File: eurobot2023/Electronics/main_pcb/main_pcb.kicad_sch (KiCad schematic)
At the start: 34 parts, among them IC1 CD74HCT125M96, IC2 SN74LVC126ADR, J1 PI40HAT, J10 Conn_01x02_Male, J11 MagneticEncoder, J12 Conn_01x07_Male, J13 MagneticEncoder, J14 Conn_01x03_Male, J15 Conn_01x02_Male, J2 Conn_01x02_Male, J3 Conn_01x02_Male, J4 Conn_01x02_Male, J5 Conn_01x02_Male, J6 Conn_01x02_Male, J7 Conn_01x02_Male, J9 22-03-5035, P1 R-78Bxx-2.0, P2 Amazon 5A stepdown, U1 MCP2515-xSO, U2 TJA1049T, U3 PCA9306D, U4 Pololu_MAX14870, U5 PCA9685PW

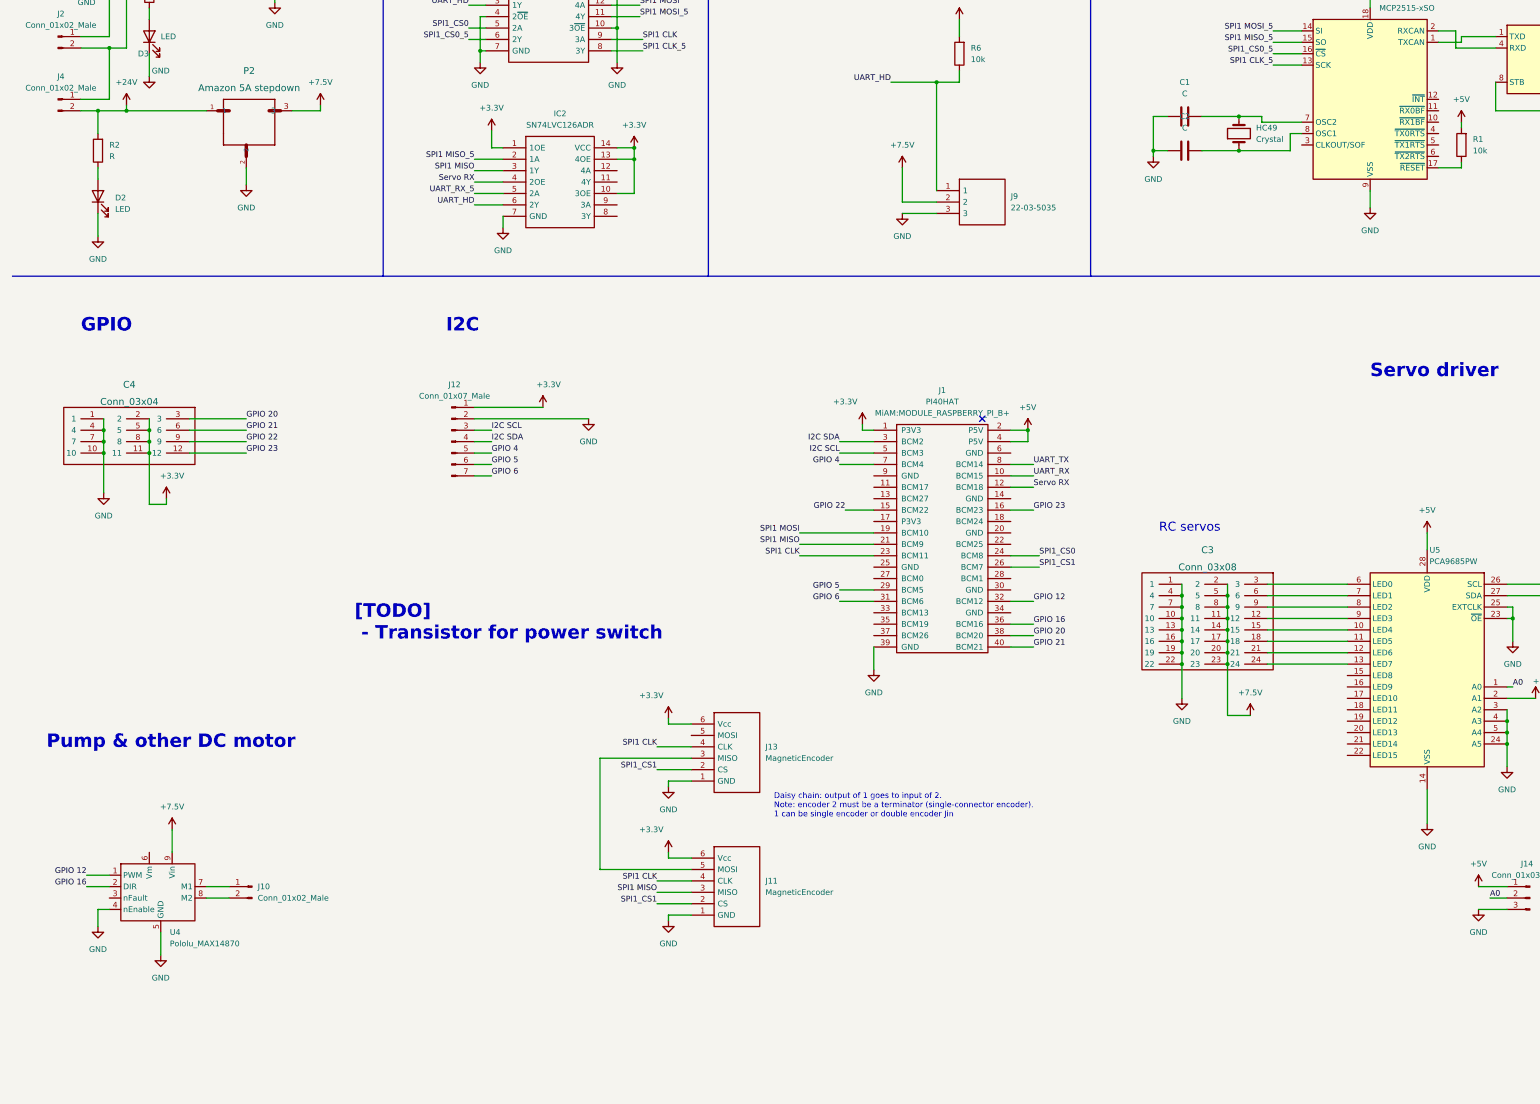
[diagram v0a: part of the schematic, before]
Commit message: Electronics: fixup to SecondaryPCB and update MainPCB schematic.
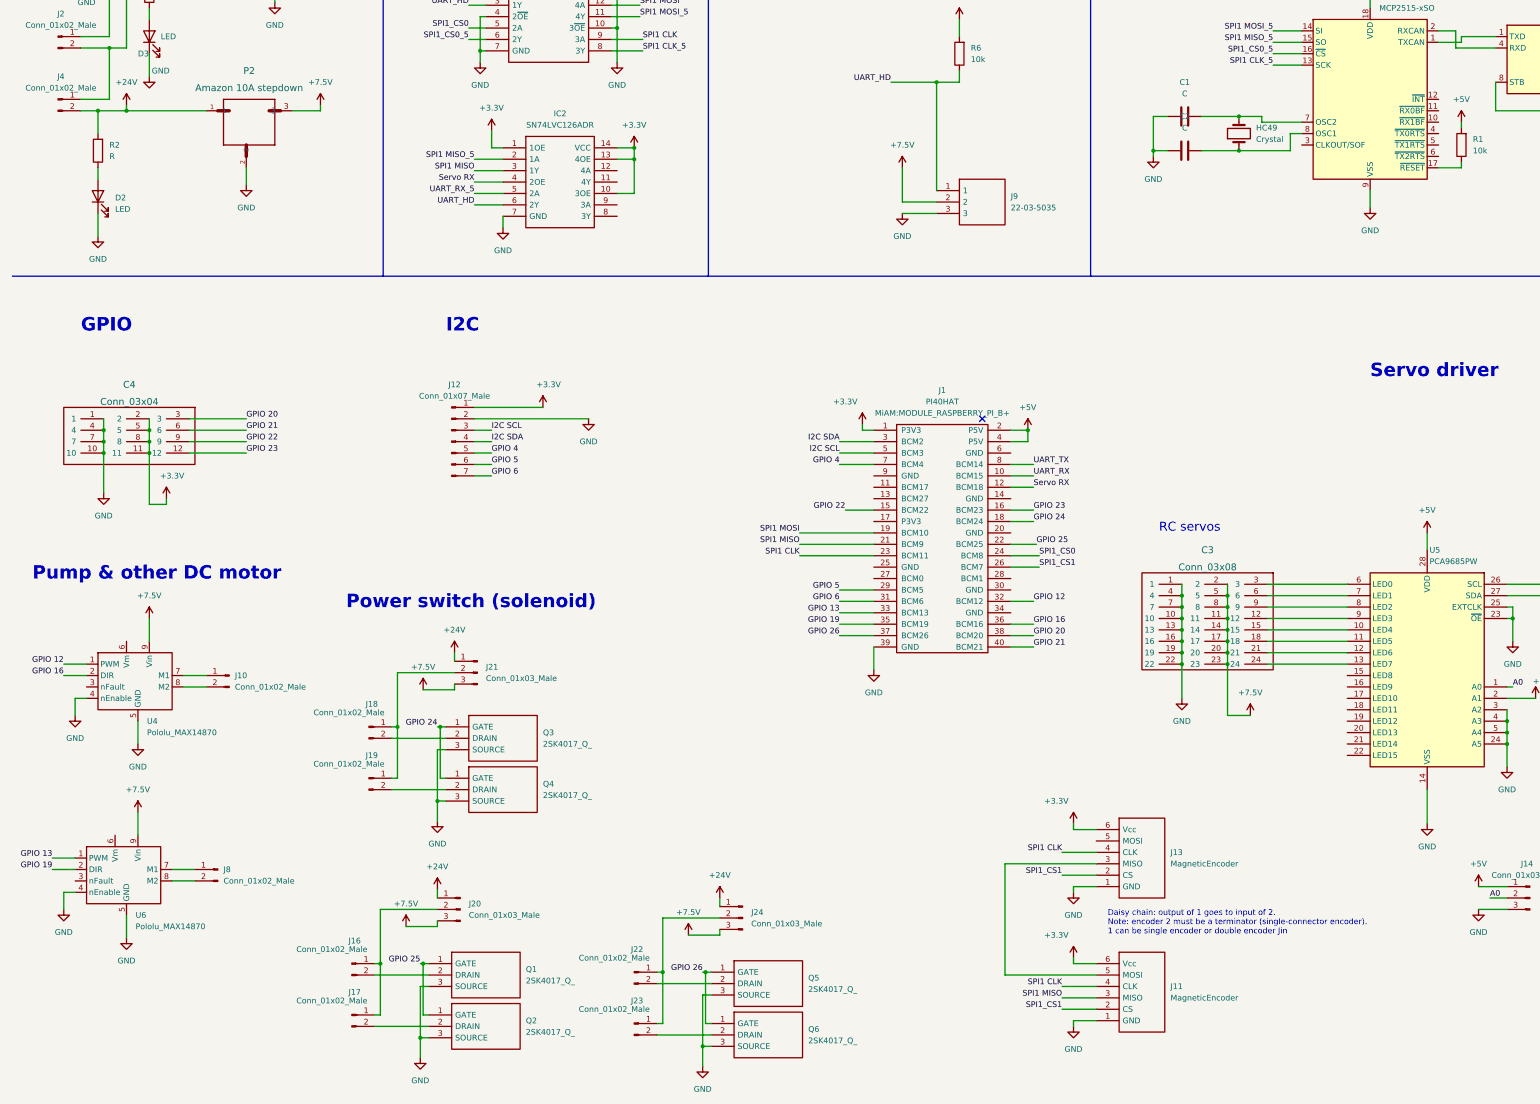
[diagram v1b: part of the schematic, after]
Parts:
- removed P2: Amazon 5A stepdown, MiAM:StepDown5A, symbol MiAM:Amazon 5A stepdown
- added J16, J17, J18, J19, J22, J23, J8: Conn_01x02_Male, Connector_PinHeader_2.54mm:PinHeader_1x02_P2.54mm_Vertical, symbol Connector:Conn_01x02_Male
- added J20, J21, J24: Conn_01x03_Male, Connector_PinHeader_2.54mm:PinHeader_1x03_P2.54mm_Vertical, symbol Connector:Conn_01x03_Male
- added P2: Amazon 10A stepdown, MiAM:StepDown10A, symbol MiAM:Amazon 10A stepdown
- added Q1, Q2, Q3, Q4, Q5, Q6: 2SK4017_Q_, TO230P250X650X900-3P, symbol MiAM:2SK4017_Q_
- added U6: Pololu_MAX14870, MiAM:PololuMAX14870, symbol MiAM:Pololu_MAX14870
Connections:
- net +24V: now also J20.1 (Pin_1), J21.1 (Pin_1), J24.1 (Pin_1), P2.1
- net +7.5V: now also J20.3 (Pin_3), J21.3 (Pin_3), J24.3 (Pin_3), P2.3, U6.9 (Vin)
- net GND: now also P2.2, Q1.3 (SOURCE), Q2.3 (SOURCE), Q3.3 (SOURCE), Q4.3 (SOURCE), Q5.3 (SOURCE), Q6.3 (SOURCE), U6.4 (nEnable), U6.5 (GND)
- net GPIO 24: now reaches J1.18 (BCM24)
- net GPIO 24: now also Q3.1 (GATE), Q4.1 (GATE)
- net GPIO 25: now reaches J1.22 (BCM25)
- net GPIO 25: now also Q1.1 (GATE), Q2.1 (GATE)
- net GPIO 13: now reaches J1.33 (BCM13)
- net GPIO 13: now also U6.1 (PWM)
- net GPIO 19: now reaches J1.35 (BCM19)
- net GPIO 19: now also U6.2 (DIR)
- net GPIO 26: now reaches J1.37 (BCM26)
- net GPIO 26: now also Q5.1 (GATE), Q6.1 (GATE)
- new net: J18.2 (Pin_2), Q3.2 (DRAIN)
- new net: J18.1 (Pin_1), J19.1 (Pin_1), J21.2 (Pin_2)
- new net: J19.2 (Pin_2), Q4.2 (DRAIN)
- new net: J16.1 (Pin_1), J17.1 (Pin_1), J20.2 (Pin_2)
- new net: J16.2 (Pin_2), Q1.2 (DRAIN)
- new net: J22.1 (Pin_1), J23.1 (Pin_1), J24.2 (Pin_2)
- new net: J22.2 (Pin_2), Q5.2 (DRAIN)
- new net: J23.2 (Pin_2), Q6.2 (DRAIN)
- new net: J17.2 (Pin_2), Q2.2 (DRAIN)
- new net: J8.1 (Pin_1), U6.7 (M1)
- new net: J8.2 (Pin_2), U6.8 (M2)
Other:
- note added: "Power switch (solenoid)"
- note removed: "[TODO] - Transistor for power switch"
- moved on the sheet: J10, J11, J13, U4

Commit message: Main PCB: update component placement.
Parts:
- removed J16, J17, J18, J19, J22, J23: Conn_01x02_Male, Connector_PinHeader_2.54mm:PinHeader_1x02_P2.54mm_Vertical, symbol Connector:Conn_01x02_Male
- added J16, J17, J18: Conn_02x02_Odd_Even, Connector_PinHeader_2.54mm:PinHeader_2x02_P2.54mm_Vertical, symbol Connector_Generic:Conn_02x02_Odd_Even
- R1, R6: footprint Resistor_THT:R_Axial_DIN0309_L9.0mm_D3.2mm_P12.70mm_Horizontal -> Resistor_SMD:R_0805_2012Metric
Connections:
- net at Q3.2 (DRAIN): now also J17.2 (Pin_2)
- net at J21.2 (Pin_2): now also J17.1 (Pin_1), J17.3 (Pin_3)
- net at Q4.2 (DRAIN): now also J17.4 (Pin_4)
- net at J20.2 (Pin_2): now also J16.1 (Pin_1), J16.3 (Pin_3)
- net at Q1.2 (DRAIN): now also J16.2 (Pin_2)
- net at J24.2 (Pin_2): now also J18.1 (Pin_1), J18.3 (Pin_3)
- net at Q5.2 (DRAIN): now also J18.2 (Pin_2)
- net at Q6.2 (DRAIN): now also J18.4 (Pin_4)
- net at Q2.2 (DRAIN): now also J16.4 (Pin_4)

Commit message: Route main pcb
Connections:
- net UART_RX_5 is gone; now on net UART_HD: IC2.5 (2A)
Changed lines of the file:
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@@
     (effects (font (size 1.27 1.27)) (justify left bottom))
   )
-  (label "UART_RX_5" (at 115.57 83.185 180)
+  (label "UART_HD" (at 115.57 83.185 180)
     (effects (font (size 1.27 1.27)) (justify right bottom))
   )

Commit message: Electronics: correct PCB schematic and component references.
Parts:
- added I2C1, I2C2: Conn_01x05_Male, Connector_PinHeader_2.54mm:PinHeader_1x05_P2.54mm_Vertical, symbol Connector:Conn_01x05_Male
- added R4: 10k, Resistor_SMD:R_0805_2012Metric, symbol Device:R
- added R5, R7: 5k, Resistor_THT:R_Axial_DIN0309_L9.0mm_D3.2mm_P12.70mm_Horizontal, symbol Device:R
- added R8: 120, Resistor_THT:R_Axial_DIN0309_L9.0mm_D3.2mm_P12.70mm_Horizontal, symbol Device:R
- added R9: 200k, Resistor_THT:R_Axial_DIN0309_L9.0mm_D3.2mm_P12.70mm_Horizontal, symbol Device:R
- C1, C2: footprint Capacitor_THT:C_Rect_L10.0mm_W2.5mm_P7.50mm_MKS4 -> Capacitor_THT:C_Disc_D8.0mm_W5.0mm_P10.00mm
- HC49: Field4 693-8819 -> (none); RS (none) -> 693-8819
- P1: RS Recom R-78B5.0-2.0 -> 139-2959
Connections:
- net +3.3V: now also I2C1.1 (Pin_1), I2C2.1 (Pin_1)
- net +5V: now also R4.2, R5.2, R7.2, R9.2; no longer U3.7 (VREF2)
- net GND: now also I2C1.2 (Pin_2), I2C2.2 (Pin_2)
- net I2C SCL: now also I2C1.3 (Pin_3), I2C2.3 (Pin_3)
- net I2C SDA: now also I2C1.4 (Pin_4), I2C2.4 (Pin_4)
- net UART_RX: now also IC2.6 (2Y), R4.1
- net at J15.2 (Pin_2), J7.2 (Pin_2), U2.6 (CANL): now also R8.1
- net at J15.1 (Pin_1), J7.1 (Pin_1), U2.7 (CANH): now also R8.2
- net GPIO 17: now reaches J1.11 (BCM17)
- net GPIO 17: now also I2C1.5 (Pin_5)
- net GPIO 27: now reaches J1.13 (BCM27)
- net GPIO 27: now also I2C2.5 (Pin_5)
- net at U3.6 (SCL2), U5.26 (SCL): now also R7.1
- net at U3.5 (SDA2), U5.27 (SDA): now also R5.1
- net at U3.8 (EN): now also U3.7 (VREF2), R9.1
- net Servo RX renamed Servo DIR
- net UART_HD renamed UART_HalfDuplex
- net UART_HalfDuplex: no longer IC2.6 (2Y)
- no-connect marks 1 -> 0
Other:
- note added: "Encoders"
- note added: "Raspberry Pi"
- moved on the sheet: C3, HC49, IC2, J1, J10, J11, J12, J13, J14, J15, J16, J17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

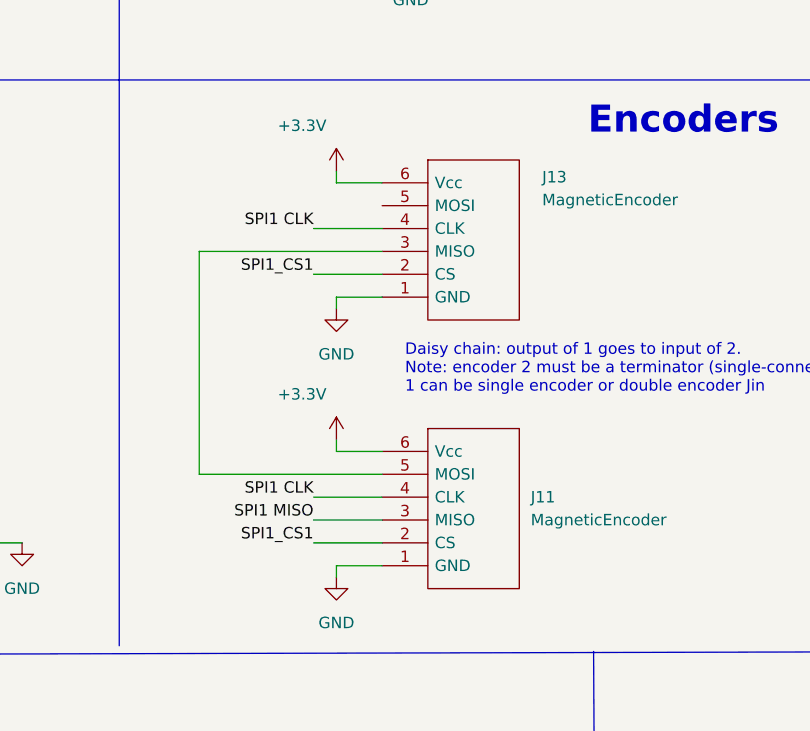
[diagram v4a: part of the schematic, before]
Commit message: Electronics: update PCB
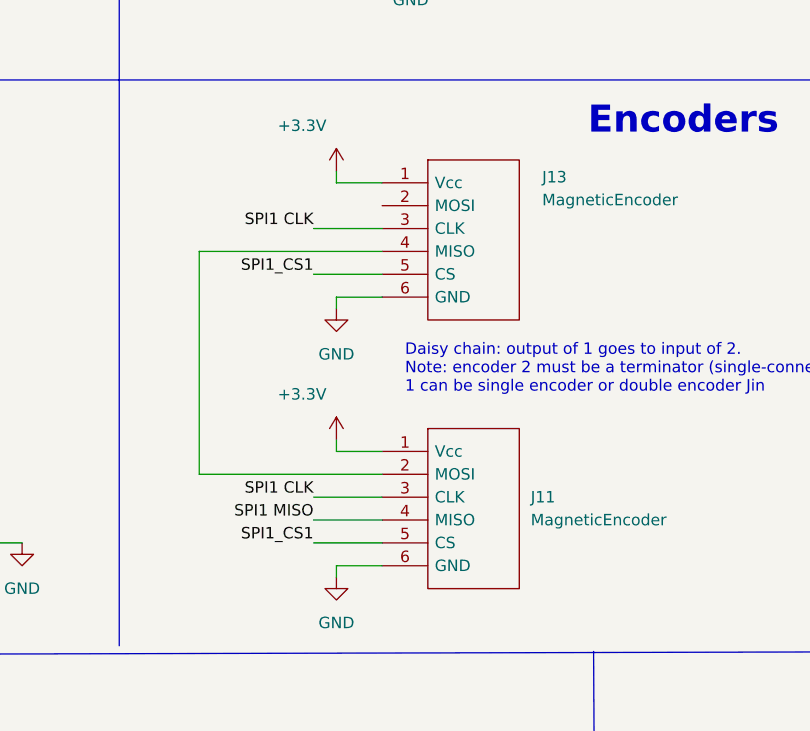
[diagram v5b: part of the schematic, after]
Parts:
- R2, R3, R5, R7, R8, R9: footprint Resistor_THT:R_Axial_DIN0309_L9.0mm_D3.2mm_P12.70mm_Horizontal -> Resistor_SMD:R_0805_2012Metric
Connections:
- net +3.3V: now also J11.1 (Vcc), J13.1 (Vcc); no longer J11.6 (Vcc), J13.6 (Vcc)
- net GND: now also J11.6 (GND), J13.6 (GND); no longer J11.1 (GND), J13.1 (GND)
- net SPI1 CLK: now also J11.3 (CLK), J13.3 (CLK); no longer J11.4 (CLK), J13.4 (CLK)
- net SPI1 MISO: now also J11.4 (MISO); no longer J11.3 (MISO)
- net SPI1_CS1: now also J11.5 (CS), J13.5 (CS); no longer J11.2 (CS), J13.2 (CS)
- new net: J11.2 (MOSI), J13.4 (MISO)
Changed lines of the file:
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@@
       (effects (font (size 1.27 1.27)) (justify right))
     )
-    (property "Footprint" "Resistor_THT:R_Axial_DIN0309_L9.0mm_D3.2mm_P12.70mm_Horizontal" (id 2) (at 363.728 135.255 90)
+    (property "Footprint" "Resistor_SMD:R_0805_2012Metric" (id 2) (at 363.728 135.255 90)
       (effects (font (size 1.27 1.27)) hide)
     )
@@
       (effects (font (size 1.27 1.27)) (justify right))
     )
-    (property "Footprint" "Resistor_THT:R_Axial_DIN0309_L9.0mm_D3.2mm_P12.70mm_Horizontal" (id 2) (at 371.983 59.69 90)
+    (property "Footprint" "Resistor_SMD:R_0805_2012Metric" (id 2) (at 371.983 59.69 90)
       (effects (font (size 1.27 1.27)) hide)
     )
@@
       (effects (font (size 1.27 1.27)) (justify right))
     )
-    (property "Footprint" "Resistor_THT:R_Axial_DIN0309_L9.0mm_D3.2mm_P12.70mm_Horizontal" (id 2) (at 373.888 171.45 90)
+    (property "Footprint" "Resistor_SMD:R_0805_2012Metric" (id 2) (at 373.888 171.45 90)
       (effects (font (size 1.27 1.27)) hide)
     )
@@
       (effects (font (size 1.27 1.27)) (justify right))
     )
-    (property "Footprint" "Resistor_THT:R_Axial_DIN0309_L9.0mm_D3.2mm_P12.70mm_Horizontal" (id 2) (at 44.958 38.1 90)
+    (property "Footprint" "Resistor_SMD:R_0805_2012Metric" (id 2) (at 44.958 38.1 90)
       (effects (font (size 1.27 1.27)) hide)
     )
@@
       (effects (font (size 1.27 1.27)) (justify right))
     )
-    (property "Footprint" "Resistor_THT:R_Axial_DIN0309_L9.0mm_D3.2mm_P12.70mm_Horizontal" (id 2) (at 33.528 73.66 90)
+    (property "Footprint" "Resistor_SMD:R_0805_2012Metric" (id 2) (at 33.528 73.66 90)
       (effects (font (size 1.27 1.27)) hide)
     )
@@
     (pin "1")
   )
-  (symbol (lib_id "MiAM:MagneticEncoder") (at 196.85 113.03 0) (unit 1)
+  (symbol (lib_name "MagneticEncoder_1") (lib_id "MiAM:MagneticEncoder") (at 196.85 113.03 0) (unit 1)
     (in_bom yes) (on_board yes)
     (property "Reference" "J13" (id 0) (at 214.63 112.395 0)
@@
       (effects (font (size 1.27 1.27)) (justify right))
     )
-    (property "Footprint" "Resistor_THT:R_Axial_DIN0309_L9.0mm_D3.2mm_P12.70mm_Horizontal" (id 2) (at 358.013 135.255 90)
+    (property "Footprint" "Resistor_SMD:R_0805_2012Metric" (id 2) (at 358.013 135.255 90)
       (effects (font (size 1.27 1.27)) hide)
     )
@@
     )
     (path "/8cd8af2a-beda-42be-a4f0-fe56aaaef64a"
-      (reference "R2") (unit 1) (value "R") (footprint "Resistor_THT:R_Axial_DIN0309_L9.0mm_D3.2mm_P12.70mm_Horizontal")
+      (reference "R2") (unit 1) (value "R") (footprint "Resistor_SMD:R_0805_2012Metric")
     )
     (path "/8b0eec51-c081-4a20-b848-d05ba5caa814"
-      (reference "R3") (unit 1) (value "R") (footprint "Resistor_THT:R_Axial_DIN0309_L9.0mm_D3.2mm_P12.70mm_Horizontal")
+      (reference "R3") (unit 1) (value "R") (footprint "Resistor_SMD:R_0805_2012Metric")
     )
     (path "/06e5da98-baa3-47d3-9982-92e5a11db2fb"
@@
     )
     (path "/d9677633-2609-4662-b08f-2896cbff6611"
-      (reference "R5") (unit 1) (value "5k") (footprint "Resistor_THT:R_Axial_DIN0309_L9.0mm_D3.2mm_P12.70mm_Horizontal")
+      (reference "R5") (unit 1) (value "5k") (footprint "Resistor_SMD:R_0805_2012Metric")
     )
     (path "/0b2324c2-ebae-4281-8010-7504e7b6873a"
@@
     )
     (path "/1c3c8049-c838-4cab-9202-8349c7cb99cc"
-      (reference "R7") (unit 1) (value "5k") (footprint "Resistor_THT:R_Axial_DIN0309_L9.0mm_D3.2mm_P12.70mm_Horizontal")
+      (reference "R7") (unit 1) (value "5k") (footprint "Resistor_SMD:R_0805_2012Metric")
     )
     (path "/1fe66cd7-6577-4353-9011-f705fb7070c9"
-      (reference "R8") (unit 1) (value "120") (footprint "Resistor_THT:R_Axial_DIN0309_L9.0mm_D3.2mm_P12.70mm_Horizontal")
+      (reference "R8") (unit 1) (value "120") (footprint "Resistor_SMD:R_0805_2012Metric")
     )
     (path "/7eb499e4-be6d-4a0e-9216-676cfa8bf55c"
-      (reference "R9") (unit 1) (value "200k") (footprint "Resistor_THT:R_Axial_DIN0309_L9.0mm_D3.2mm_P12.70mm_Horizontal")
+      (reference "R9") (unit 1) (value "200k") (footprint "Resistor_SMD:R_0805_2012Metric")
     )
     (path "/93bb4413-fb88-4e19-87c6-a45362cd77c5"

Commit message: Fix main pcb
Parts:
- removed I2C1, I2C2: Conn_01x05_Male, Connector_PinHeader_2.54mm:PinHeader_1x05_P2.54mm_Vertical, symbol Connector:Conn_01x05_Male
- removed J12: Conn_01x07_Male, Connector_PinHeader_2.54mm:PinHeader_1x07_P2.54mm_Vertical, symbol Connector:Conn_01x07_Male
- added C5: Conn_03x05, MiAM:Pin_Header_Straight_3x05_Pitch2.54mm, symbol MiAM:Conn_03x05
- added R10, R11, R12: 10k, Resistor_SMD:R_0805_2012Metric, symbol Device:R
- IC2: RS Part Number 662-8601 -> SN74LVC126ADR
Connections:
- net +3.3V: now also R4.2, C5.1, C5.2, C5.3
- net +5V: no longer R4.2
- net GND: now also C5.4, C5.5, C5.6, R10.2, R11.2, R12.2
- net GPIO 17: now also C5.14
- net GPIO 24: now also R11.1
- net GPIO 25: now also R10.1
- net GPIO 26: now also R12.1
- net GPIO 27: now also C5.15
- net GPIO 4: now also C5.13
- net GPIO 5: now also C5.16
- net GPIO 6: now also C5.17
- net I2C SCL: now also C5.7, C5.8, C5.9
- net I2C SDA: now also C5.10, C5.11, C5.12
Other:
- moved on the sheet: J16, J18, J20, J21, J24, Q1, Q2, Q5, Q6, R4
